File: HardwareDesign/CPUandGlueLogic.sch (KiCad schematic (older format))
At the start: 33 parts, among them J100 Conn_02x40_Counter_Clockwise, J101 Conn_01x02, U100 74HCT245, U101 74HCT245, U102 MAX708, U103 HD6809, U104 74HCT245, U105 74HCT365, U106 74HCT00, U107 74HCT27, U108 74HCT138, U109 74HCT138, U110 74HCT138, Y100 Crystal

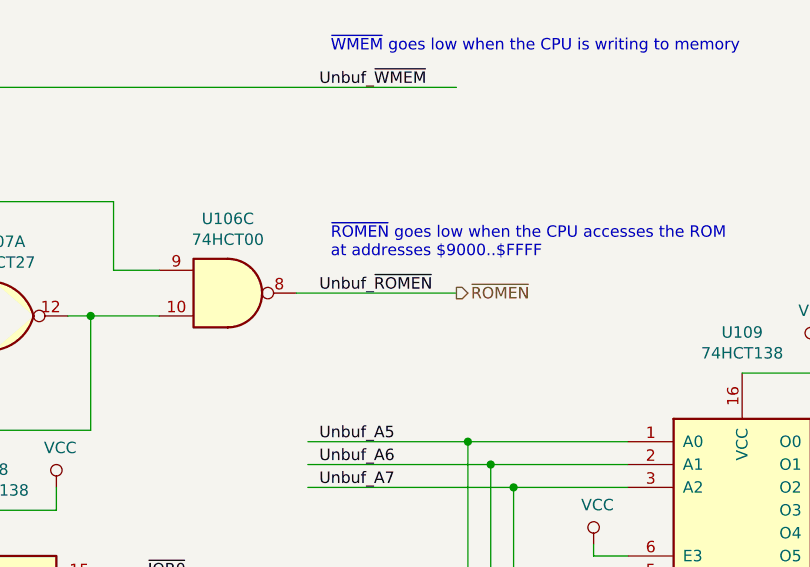
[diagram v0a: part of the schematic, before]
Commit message: -ROMEN is not buffered
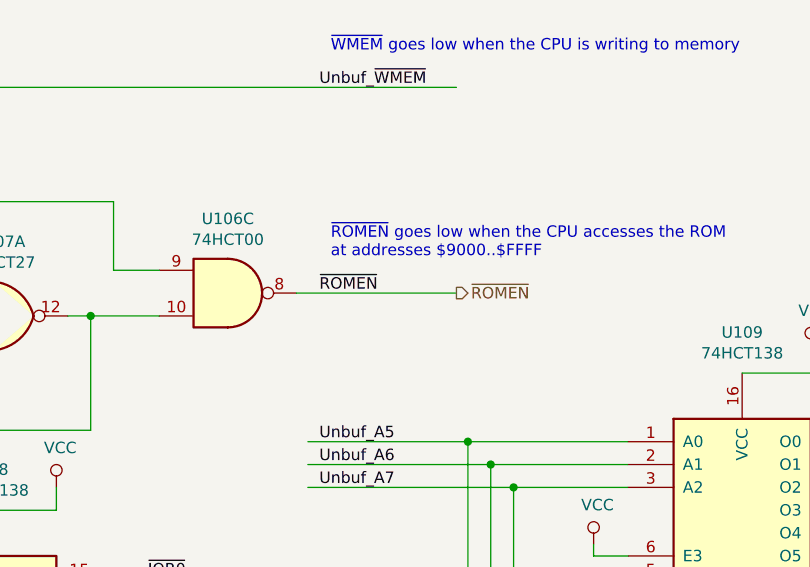
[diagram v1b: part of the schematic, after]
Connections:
- net labels removed: Unbuf_~ROMEN~
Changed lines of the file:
@@
 	9900 2650 10600 2650
 Text Label 10000 2650 0    50   ~ 0
-Unbuf_~ROMEN~
+~ROMEN~
 $Comp
 L 74xx:74LS138 U108

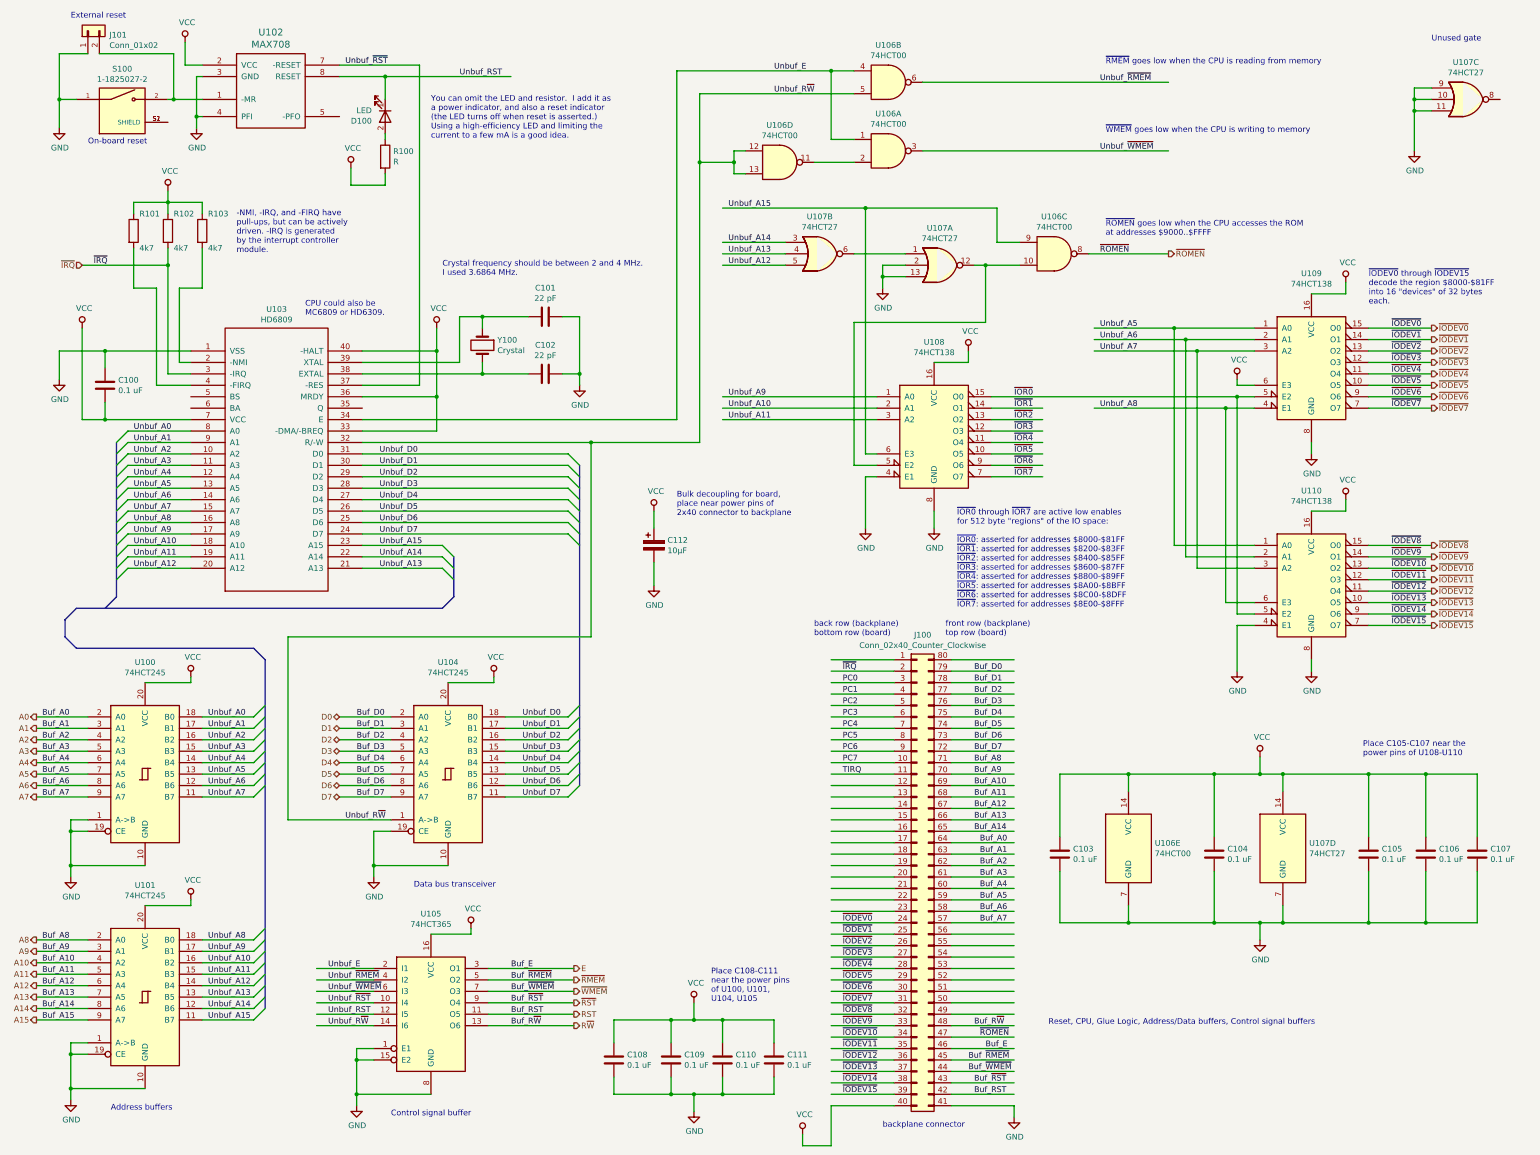
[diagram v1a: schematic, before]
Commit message: more preparations for PCB layout
More nets connected to appropriate backplane connector pin.
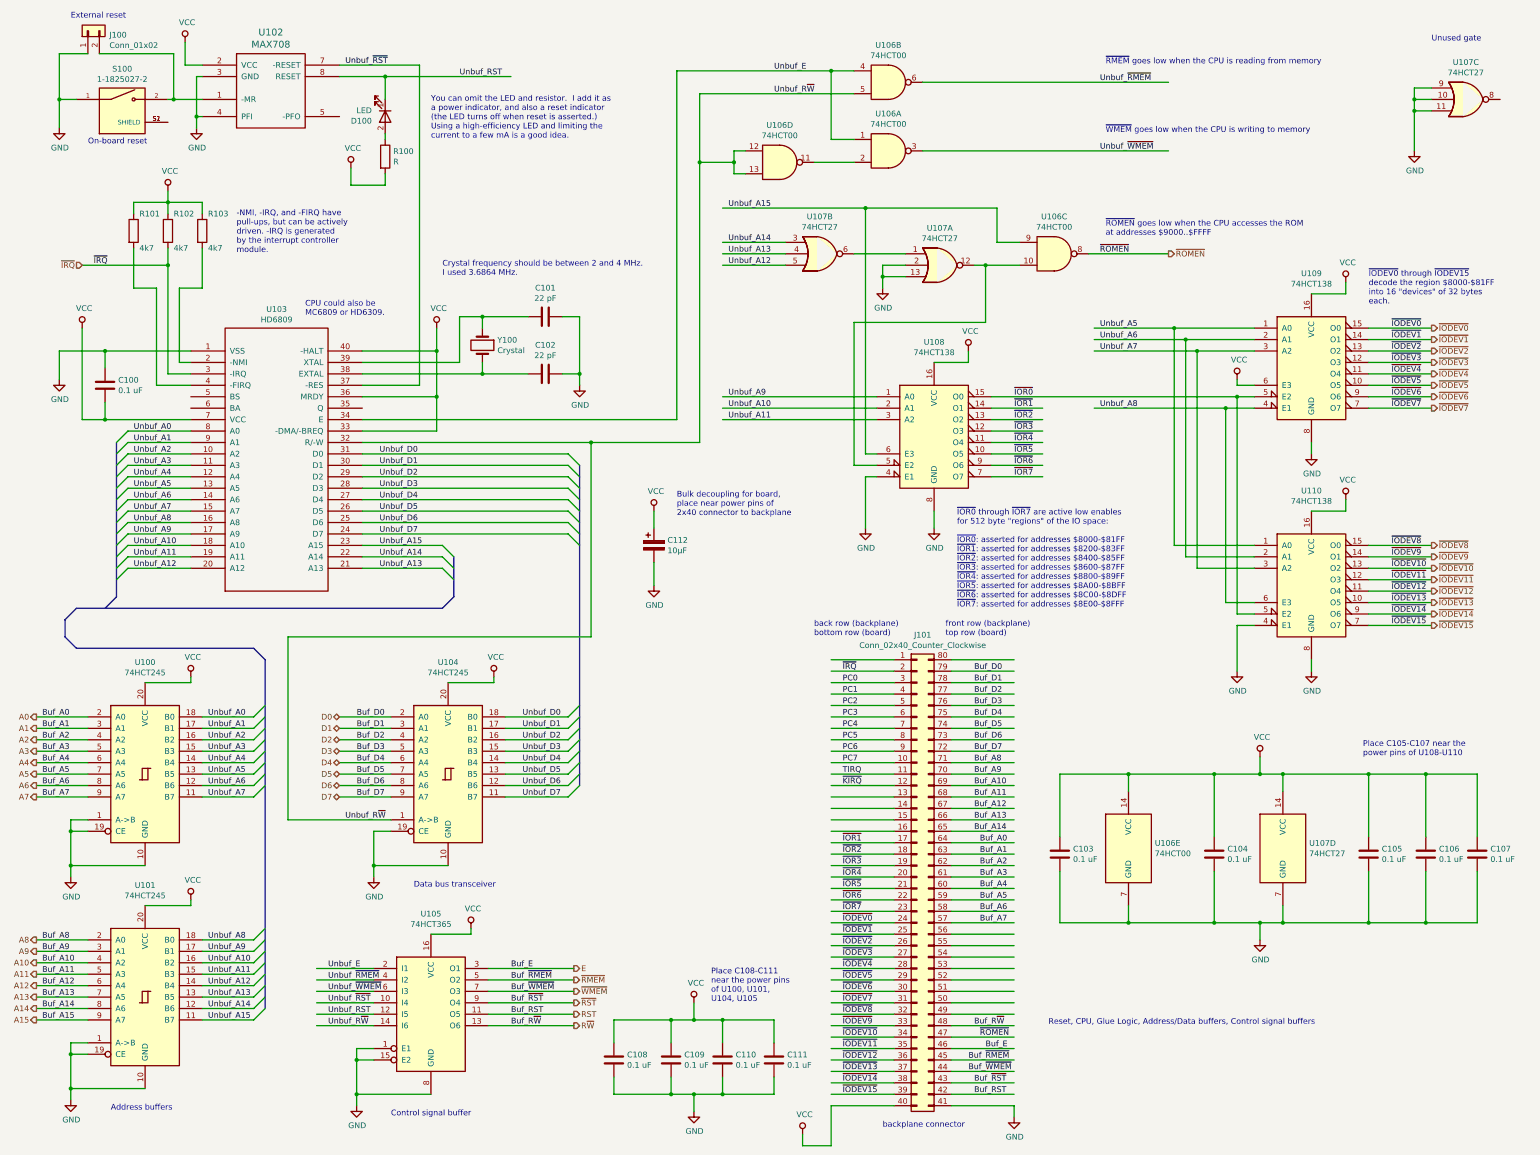
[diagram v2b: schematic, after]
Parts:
- renumbered J101 to J100, J100 to J101
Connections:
- net labels added: ~IOR0~, ~IOR1~, ~IOR2~, ~IOR3~, ~IOR4~, ~IOR5~, ~IOR6~, ~IOR7~, ~KIRQ~
- net labels removed: ~IOR0, ~IOR1, ~IOR2, ~IOR3, ~IOR4, ~IOR5, ~IOR6, ~IOR7
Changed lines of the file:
@@
 	9050 4600 9500 4600
 Text Label 9250 3900 0    50   ~ 0
-~IOR0
+~IOR0~
 Text Label 9250 4000 0    50   ~ 0
-~IOR1
+~IOR1~
 Text Label 9250 4100 0    50   ~ 0
-~IOR2
+~IOR2~
 Text Label 9250 4200 0    50   ~ 0
-~IOR3
+~IOR3~
 Text Label 9250 4300 0    50   ~ 0
-~IOR4
+~IOR4~
 Text Label 9250 4400 0    50   ~ 0
-~IOR5
+~IOR5~
 Text Label 9250 4500 0    50   ~ 0
-~IOR6
+~IOR6~
 Text Label 9250 4600 0    50   ~ 0
-~IOR7
+~IOR7~
 Wire Wire Line
 	12350 3300 12900 3300
@@
 $EndComp
 $Comp
-L Connector_Generic:Conn_02x40_Counter_Clockwise J100
+L Connector_Generic:Conn_02x40_Counter_Clockwise J101
 U 1 1 60A6FC79
 P 8400 8100
-F 0 "J100" H 8450 10217 50  0000 C CNN
+F 0 "J101" H 8450 10217 50  0000 C CNN
 F 1 "Conn_02x40_Counter_Clockwise" H 8450 10126 50  0000 C CNN
 F 2 "" H 8400 8100 50  0001 C CNN
@@
 backplane connector
 $Comp
-L Connector_Generic:Conn_01x02 J101
+L Connector_Generic:Conn_01x02 J100
 U 1 1 60A78691
 P 1150 700
-F 0 "J101" V 1114 512 50  0000 R CNN
+F 0 "J100" V 1114 512 50  0000 R CNN
 F 1 "Conn_01x02" V 1023 512 50  0000 R CNN
 F 2 "" H 1150 700 50  0001 C CNN
@@
 Wire Wire Line
 	6700 4100 8050 4100
+Text Label 7750 7800 0    50   ~ 0
+~IOR1~
+Text Label 7750 7900 0    50   ~ 0
+~IOR2~
+Text Label 7750 8000 0    50   ~ 0
+~IOR3~
+Text Label 7750 8100 0    50   ~ 0
+~IOR4~
+Text Label 7750 8200 0    50   ~ 0
+~IOR5~
+Text Label 7750 8300 0    50   ~ 0
+~IOR6~
+Text Label 7750 8400 0    50   ~ 0
+~IOR7~
+Text Label 7750 7300 0    50   ~ 0
+~KIRQ~
 Wire Bus Line
 	1050 5750 4250 5750

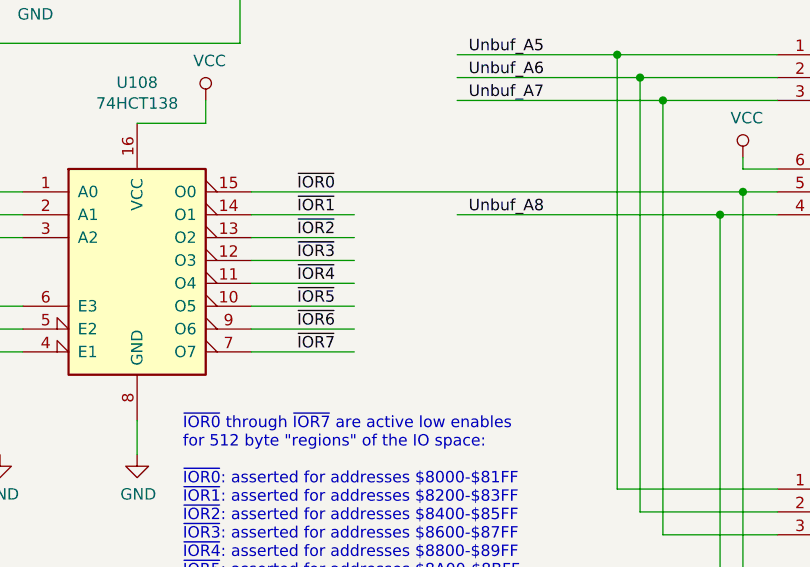
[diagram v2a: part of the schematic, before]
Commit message: more preparations for PCB layout
Make sure all nets connected to backplane connector pins are
labeled correctly.

Add bulk decoupling caps for each backplane connector.

Make keyboard interrupt be -IRQ5 rather than -IRQ7.
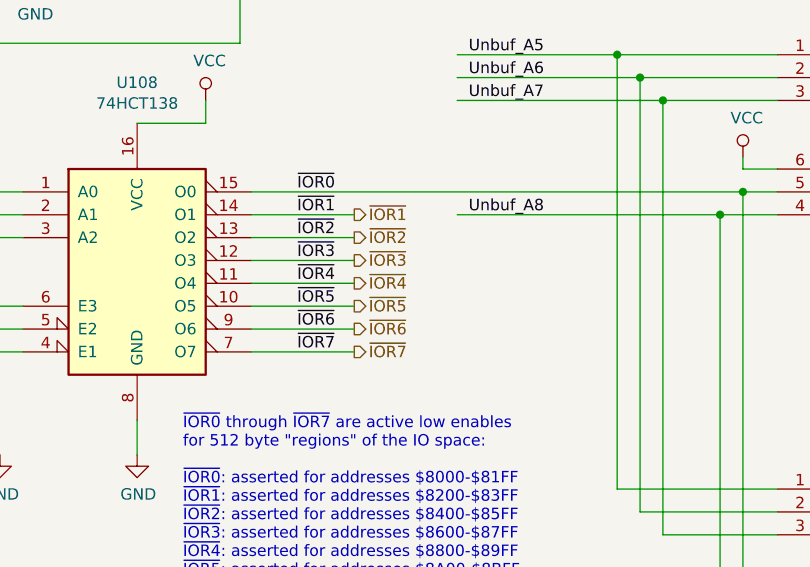
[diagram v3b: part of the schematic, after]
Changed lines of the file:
@@
 Text Label 7750 7300 0    50   ~ 0
 ~KIRQ~
+Text HLabel 9500 4000 2    50   Output ~ 0
+~IOR1~
+Text HLabel 9500 4100 2    50   Output ~ 0
+~IOR2~
+Text HLabel 9500 4200 2    50   Output ~ 0
+~IOR3~
+Text HLabel 9500 4300 2    50   Output ~ 0
+~IOR4~
+Text HLabel 9500 4400 2    50   Output ~ 0
+~IOR5~
+Text HLabel 9500 4500 2    50   Output ~ 0
+~IOR6~
+Text HLabel 9500 4600 2    50   Output ~ 0
+~IOR7~
 Wire Bus Line
 	1050 5750 4250 5750

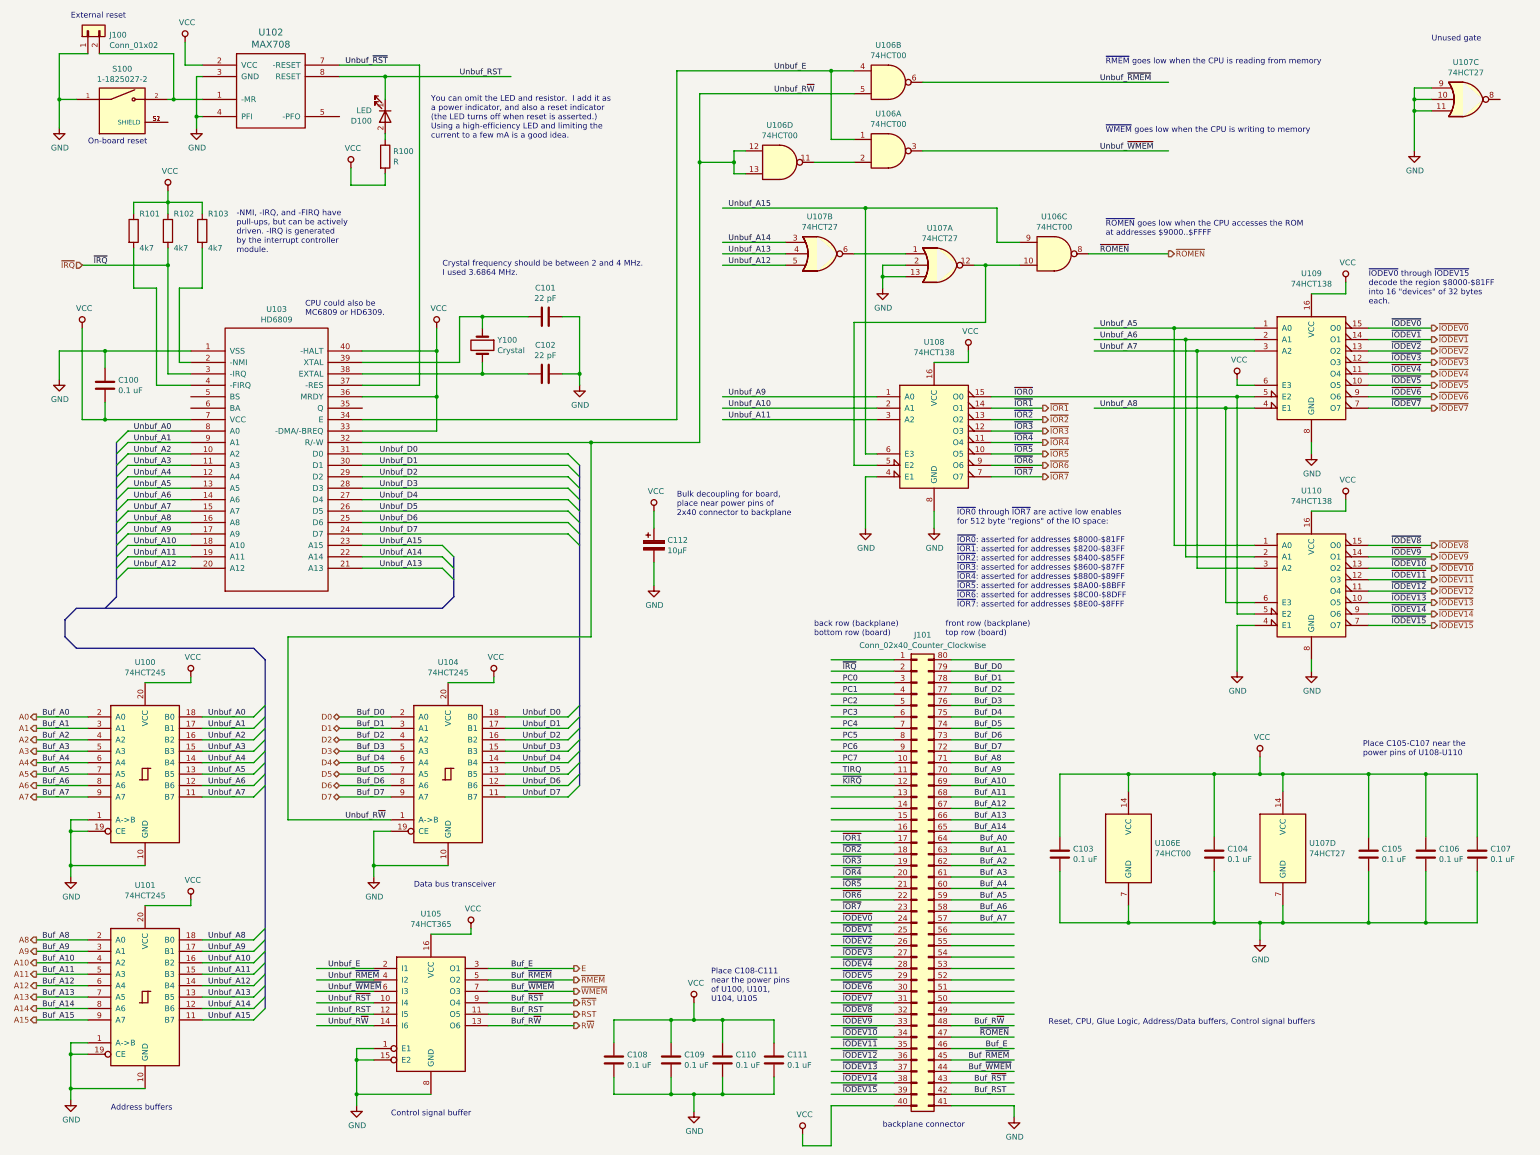
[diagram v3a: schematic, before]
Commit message: renumber capacitors to match IC numbers
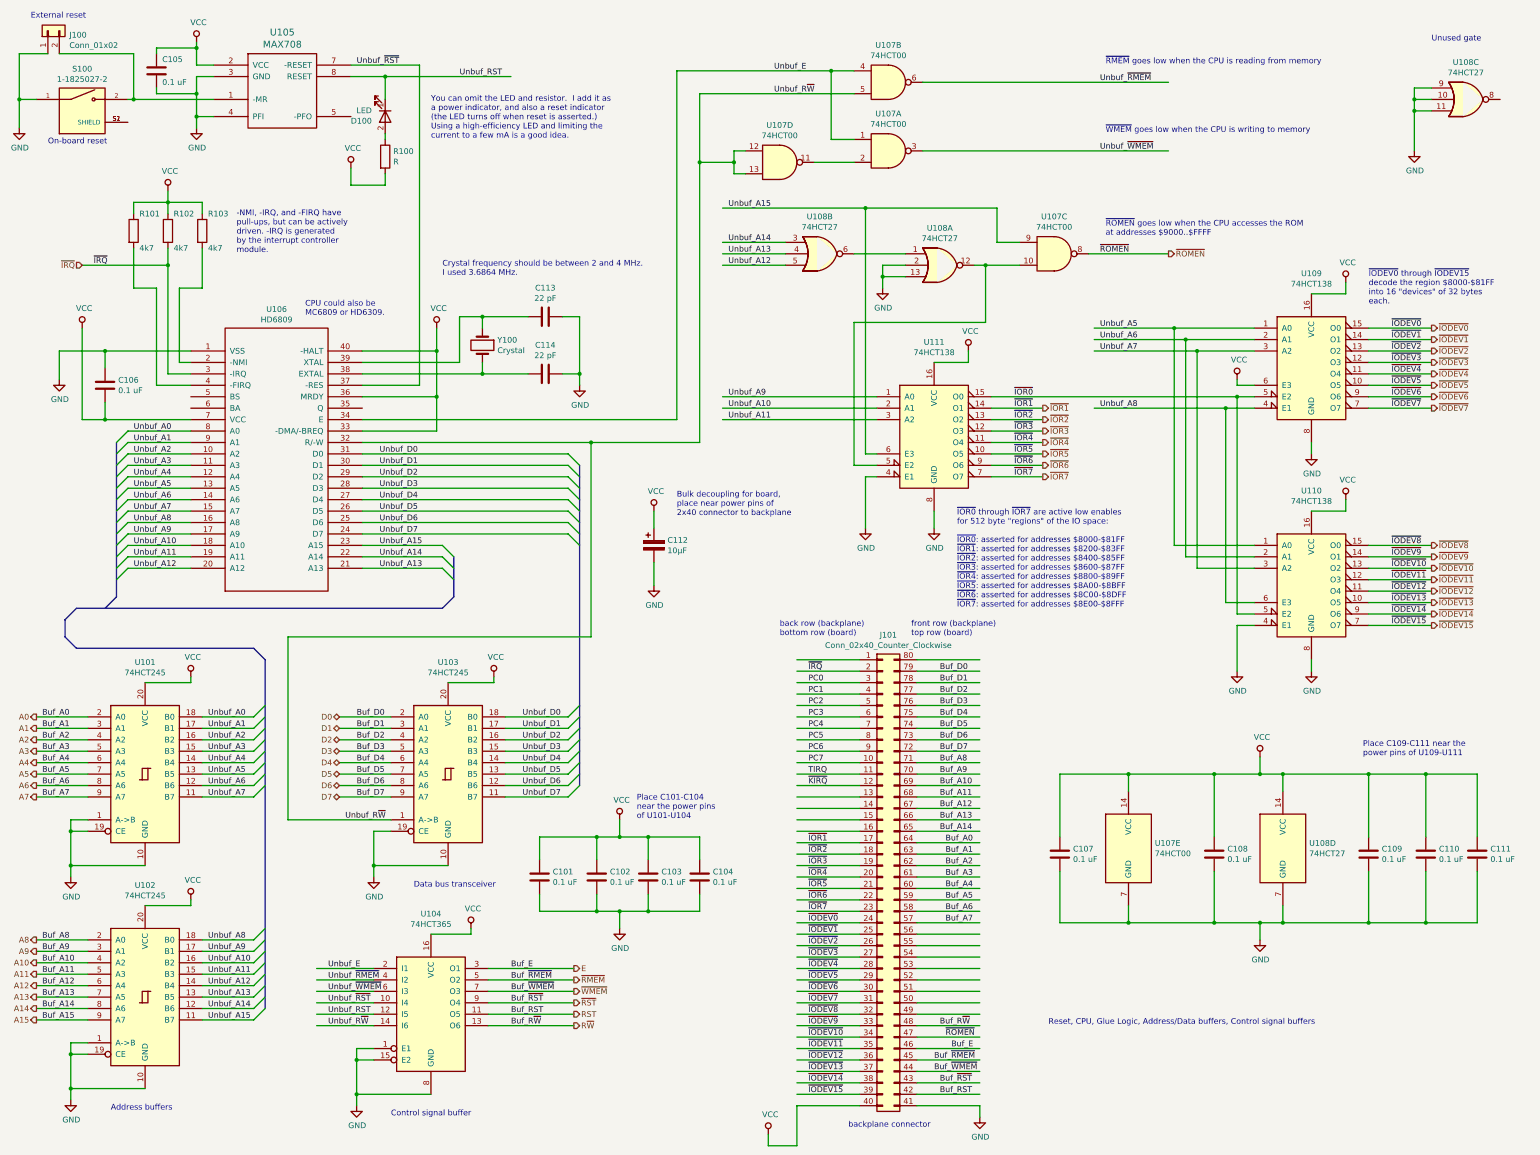
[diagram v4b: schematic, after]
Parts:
- added C105: 0.1 uF, symbol device:C
- renumbered C108 to C101, C109 to C102, C110 to C103, C111 to C104, C100 to C106, C103 to C107, C104 to C108, C105 to C109, C106 to C110, C107 to C111, C101 to C113, C102 to C114, U100 to U101, U101 to U102, U104 to U103, U105 to U104, U102 to U105, U103 to U106, U106 to U107, U107 to U108, U108 to U111
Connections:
- wire segments 427 -> 433
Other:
- note added: "Place C101-C104\nnear the power pins\nof U101-U104"
- note added: "Place C109-C111 near the\npower pins of U109-U111"
- note removed: "Place C105-C107 near the\npower pins of U108-U110"
- note removed: "Place C108-C111\nnear the power pins\nof U100, U101,\nU104, U105"
- moved on the sheet: C101, C102, C103, C104, J100, J101, S100, U105
